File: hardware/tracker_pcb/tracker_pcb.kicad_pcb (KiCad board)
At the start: 4 copper layers, 132.8 x 54.5 mm, 99 parts, among them IC1 DRV8244SQRYJRQ1, IC2 DRV8244SQRYJRQ1, IC3 THVD1426DRLR, IC4 WIO-SX1262, J1 JL308-25412G01, J2 B6B-PH-K-S, J3 256-406, J4 USB_C_Receptacle_USB2.0_16P, J5 B4B-XH-A, Q1 LTV-817S-TA1-D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

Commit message: wip
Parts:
- removed U2: STPS30L30DJF-TR, footprint:SON_0L30DJF-TR_STM
- added CR1: V60D60C-M3/I, footprint:DPAK_60C-M3&slash_I_VIS, F.Cu at (97.6, 91.9)
- moved U4 8.27 mm to (90.3, 68.6), turned to 0 degrees
- moved C6 4.32 mm to (98.2, 77.0), turned to 0 degrees
- moved R3 3.18 mm to (90.1, 72.3)
- moved R2 3.16 mm to (90.1, 70.7)
- moved R6 1.98 mm to (95.9, 69.0), turned to -90 degrees
- moved D2 1.30 mm to (97.6, 69.0), turned to 90 degrees
- moved X1 0.25 mm to (92.5, 108.0)
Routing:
- net Net-(U4-VIN2): track 43.4 -> 56.2 mm, vias 0 -> 3
- net /VBUS: track 102.3 -> 114.4 mm, vias 5 -> 6
- net Net-(U4-PR1): track 9.34 -> 3.05 mm, vias 2 -> 0
- net VDD: track 56.3 -> 60.4 mm
- net GND: track 5.16 -> 7.30 mm, vias 288 -> 293
- net VRPP: vias 117 -> 114
- net /Power/VRAW: vias 0 -> 10
- added copper zone on B.Cu, net /Power/VRAW
- added copper zone on In2.Cu, net /Power/VRAW
- removed copper zone on F.Cu, net VDD

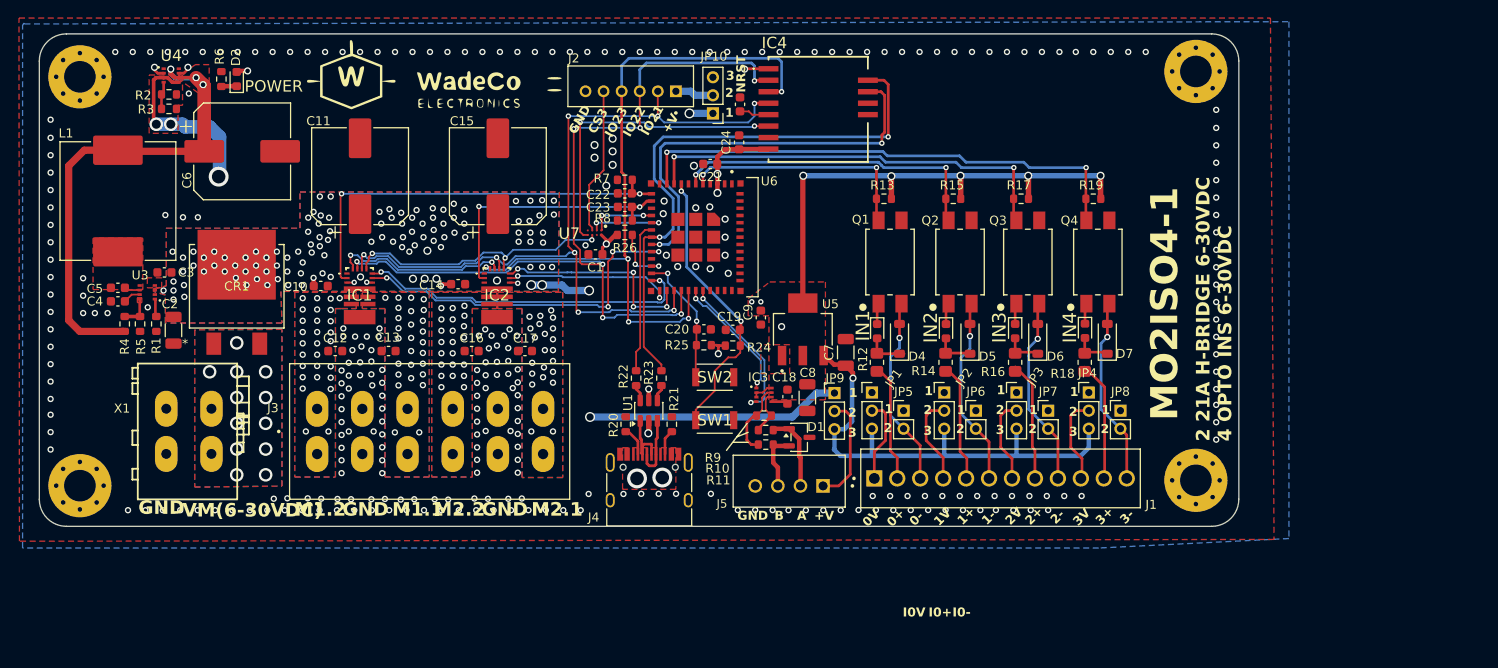
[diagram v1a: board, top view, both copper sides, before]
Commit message: Add jst xh for inputs
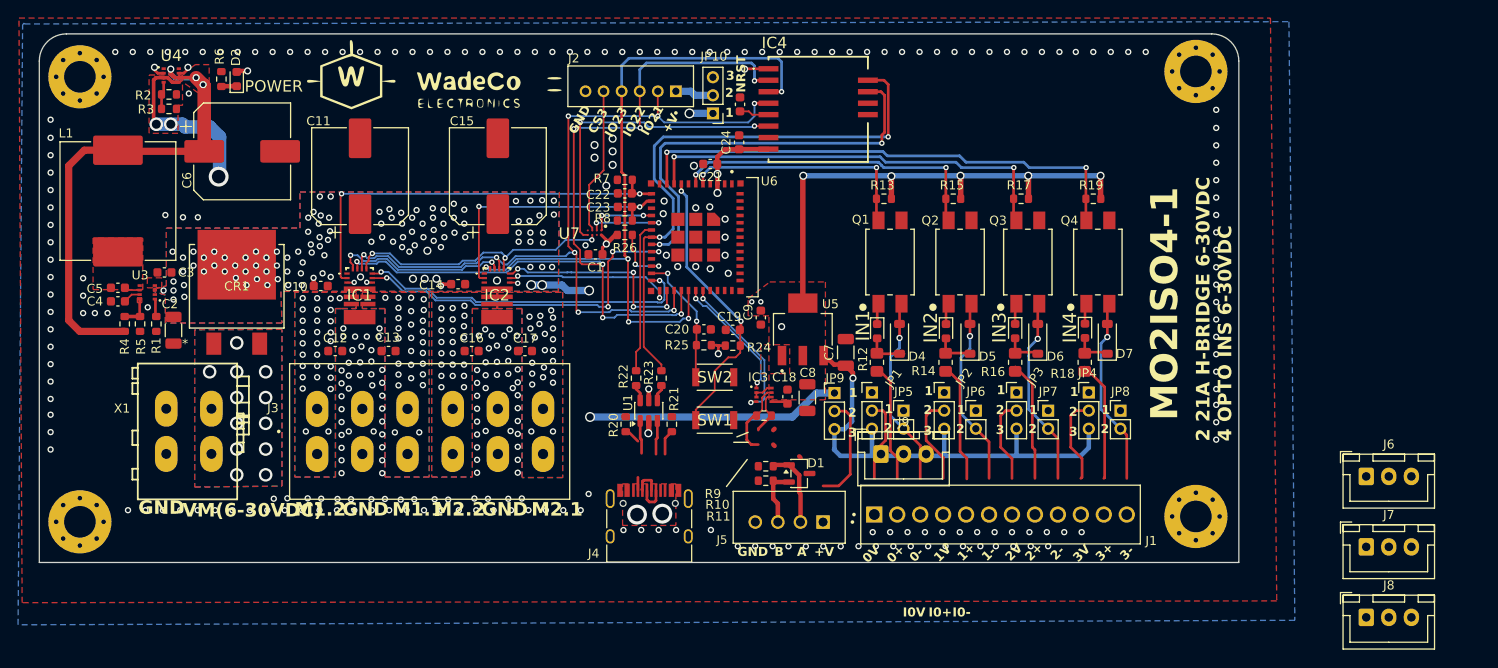
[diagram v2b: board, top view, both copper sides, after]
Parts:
- added J6: B3B-XH-A(LF)(SN), Connector_JST:JST_XH_B3B-XH-A_1x03_P2.50mm_Vertical, F.Cu at (222.6, 113.0)
- added J7: B3B-XH-A(LF)(SN), Connector_JST:JST_XH_B3B-XH-A_1x03_P2.50mm_Vertical, F.Cu at (222.6, 120.8)
- added J8: B3B-XH-A(LF)(SN), Connector_JST:JST_XH_B3B-XH-A_1x03_P2.50mm_Vertical, F.Cu at (222.6, 128.6)
- added J9: B3B-XH-A(LF)(SN), Connector_JST:JST_XH_B3B-XH-A_1x03_P2.50mm_Vertical, F.Cu at (168.9, 110.5)
- moved D1 4.00 mm to (159.8, 112.7)
- moved H2 4.00 mm to (203.8, 117.4)
- moved H3 4.00 mm to (80.2, 118.0)
- moved J1 4.00 mm to (182.1, 117.2)
- moved J4 4.00 mm to (143.2, 118.6)
- moved J5 4.00 mm to (158.7, 117.5)
- moved R10 4.00 mm to (156.2, 111.8)
- moved R11 4.00 mm to (156.2, 113.5)
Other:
- board size 132.8 x 54.5 mm -> 132.8 x 58.5 mm

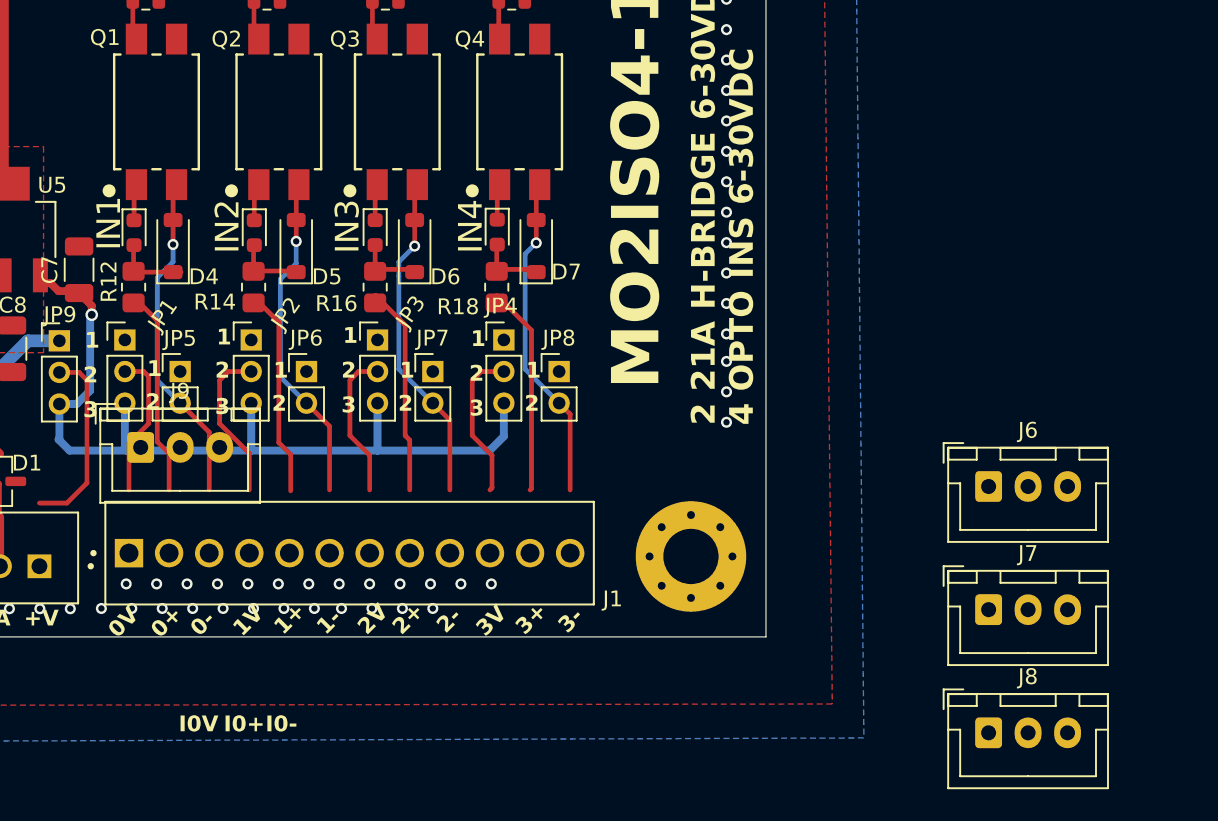
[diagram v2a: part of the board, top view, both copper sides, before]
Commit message: Add "hardware interlock" option to use iso ins 1-4 as hardware interlock for HBRDIGE PWM signals
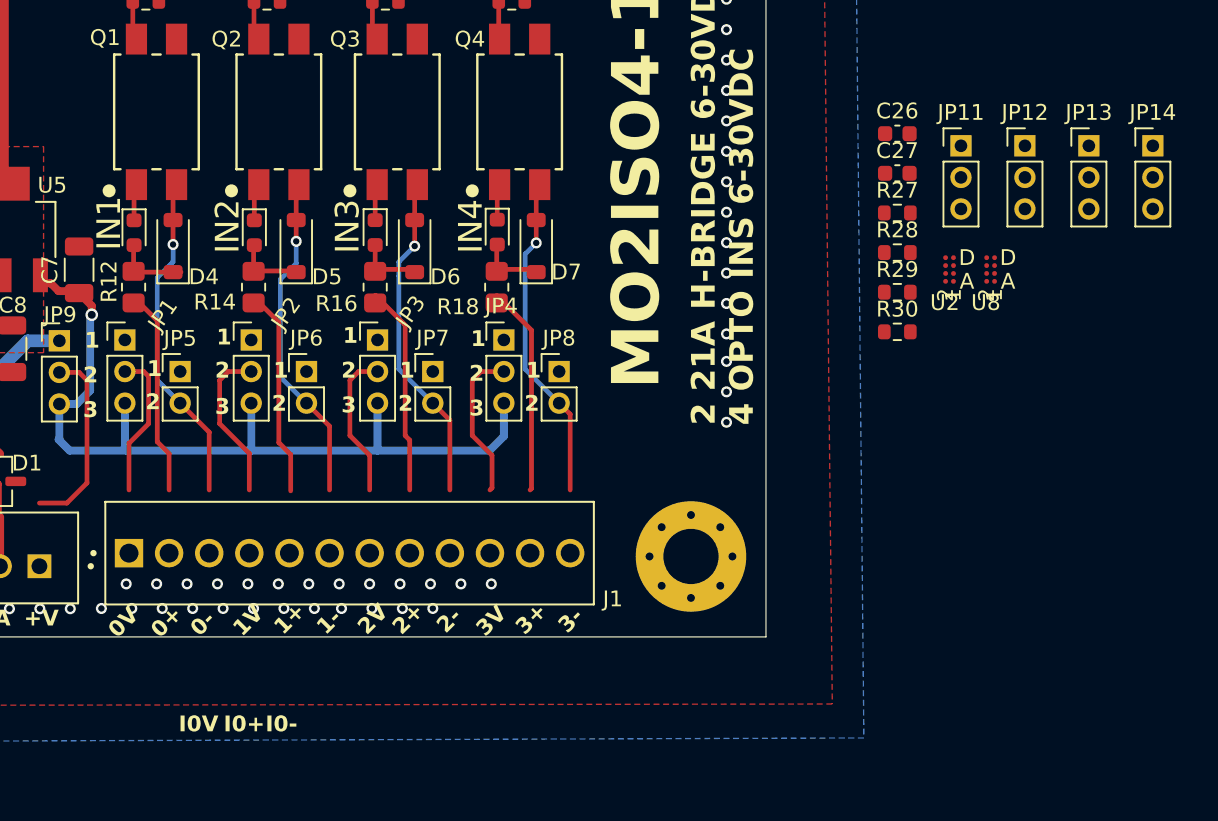
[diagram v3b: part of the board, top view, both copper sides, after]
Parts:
- removed J6, J7, J8, J9: B3B-XH-A(LF)(SN), Connector_JST:JST_XH_B3B-XH-A_1x03_P2.50mm_Vertical
- added C26: 100nF, Capacitor_SMD:C_0603_1608Metric, F.Cu at (216.8, 90.6)
- added C27: 100nF, Capacitor_SMD:C_0603_1608Metric, F.Cu at (216.8, 93.1)
- added JP11: Jumper_3_Open, Connector_PinHeader_2.00mm:PinHeader_1x03_P2.00mm_Vertical, F.Cu at (220.8, 91.4)
- added JP12: Jumper_3_Open, Connector_PinHeader_2.00mm:PinHeader_1x03_P2.00mm_Vertical, F.Cu at (224.9, 91.4)
- added JP13: Jumper_3_Open, Connector_PinHeader_2.00mm:PinHeader_1x03_P2.00mm_Vertical, F.Cu at (228.9, 91.4)
- added JP14: Jumper_3_Open, Connector_PinHeader_2.00mm:PinHeader_1x03_P2.00mm_Vertical, F.Cu at (233.0, 91.4)
- added R27: 47k, Resistor_SMD:R_0603_1608Metric, F.Cu at (216.8, 95.7)
- added R28: 47k, Resistor_SMD:R_0603_1608Metric, F.Cu at (216.8, 98.2)
- added R29: 47k, Resistor_SMD:R_0603_1608Metric, F.Cu at (216.8, 100.7)
- added R30: 47k, Resistor_SMD:R_0603_1608Metric, F.Cu at (216.8, 103.2)
- added U2: SN74AUP2G125YZPR, footprint:YZP8, F.Cu at (220.1, 99.2)
- added U8: SN74AUP2G125YZPR, footprint:YZP8, F.Cu at (222.7, 99.2)
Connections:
- net /Isolated Input/ISO_GPIO renamed /ISO0
- net /Isolated Input1/ISO_GPIO renamed /ISO1
- net /Isolated Input2/ISO_GPIO renamed /ISO2
- net /Isolated Input3/ISO_GPIO renamed /ISO3
- IC1 pad 11: /M1PWMF -> /Motor Control DRV8244_1/PWMF
- IC1 pad 12: /M1PWMR -> /Motor Control DRV8244_1/PWMR
- IC2 pad 11: /M2PWMF -> /Motor Control DRV8244_2/PWMF
- IC2 pad 12: /M2PWMR -> /Motor Control DRV8244_2/PWMR

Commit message: ss changes
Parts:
- removed C22, C23, C27: 100nF, Capacitor_SMD:C_0603_1608Metric
- removed R8: 820R, Resistor_SMD:R_0603_1608Metric
- added D3: LED, LED_SMD:LED_0603_1608Metric, F.Cu at (119.3, 86.7)
- R7: value 820R -> 460
- moved U8 84.0 mm to (139.1, 91.1), turned to 180 degrees
- moved U2 80.4 mm to (139.7, 99.5), turned to 180 degrees
- moved R28 78.2 mm to (138.7, 95.1), turned to 90 degrees
- moved R27 78.0 mm to (139.2, 103.6), turned to 90 degrees
- moved R30 76.9 mm to (140.3, 95.1), turned to 90 degrees
- moved C26 76.1 mm to (141.0, 97.4)
- moved R29 76.1 mm to (140.8, 103.6), turned to 90 degrees
- moved JP12 63.2 mm to (161.8, 89.8), turned to 180 degrees
- moved JP13 63.2 mm to (165.8, 89.8), turned to 180 degrees
- moved JP11 63.1 mm to (157.8, 89.8), turned to 180 degrees
- moved JP14 63.1 mm to (169.9, 89.8), turned to 180 degrees
- moved R7 21.3 mm to (119.3, 78.9), turned to 90 degrees
- moved R13 6.18 mm to (175.4, 82.2)
- moved D4 5.01 mm to (176.0, 97.6)
- moved LED1 5.01 mm to (173.5, 96.8)
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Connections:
- net /RS485/rs485_rx renamed /ESP32-C6/RXD0
- net /RS485/rs485_tx renamed /ESP32-C6/TXD0
- net /esp32/IO6 renamed /ESP32-C6/IO6
- net /esp32/IO7 renamed /ESP32-C6/IO7
- net /esp32/NSS_CS0 renamed /ESP32-C6/NSS_CS0
- net /esp32/USB_DM renamed /ESP32-C6/USB_DM
- C26 pad 1: GND -> V33
- C26 pad 2: V33 -> GND
- IC1 pad 1: unconnected-(IC1-NFAULT-Pad1) -> /NFAULT
- IC1 pad 2: /IOUT1 -> GND
- IC2 pad 1: unconnected-(IC2-NFAULT-Pad1) -> /NFAULT
- IC2 pad 2: /IOUT2 -> GND
- JP12 pad 2: /~{HIL0} -> /~{HIL1}
- JP12 pad 3: /ISO0 -> /ISO1
- JP13 pad 2: /~{HIL0} -> /~{HIL2}
- JP13 pad 3: /ISO0 -> /ISO2
- JP14 pad 2: /~{HIL0} -> /~{HIL3}
- JP14 pad 3: /ISO0 -> /ISO3
- R7 pad 1: GND -> Net-(D3-A)
- R7 pad 2: /IOUT1 -> VDD
- U6 pad 12: /IOUT1 -> /SX_RST
- U6 pad 13: /IOUT2 -> /NFAULT
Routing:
- net VDD: track 60.4 -> 12.1 mm, vias 5 -> 6
- net /IOUT1: track 46.7 -> 0.00 mm, vias 2 -> 0
- net /NFAULT: track 0.00 -> 44.6 mm, vias 0 -> 4
- net /Motor Control DRV8244_1/PWMF: track 0.00 -> 43.2 mm, vias 0 -> 2
- net /Motor Control DRV8244_1/PWMR: track 0.00 -> 37.7 mm, vias 0 -> 2
- net /~{HIL1}: track 0.00 -> 35.7 mm, vias 0 -> 2
- net /~{HIL3}: track 0.00 -> 32.0 mm, vias 0 -> 1
- net /IOUT2: track 30.6 -> 0.00 mm, vias 2 -> 0
- net /~{HIL0}: track 0.00 -> 30.0 mm, vias 0 -> 2
- net /~{HIL2}: track 0.00 -> 29.7 mm, vias 0 -> 1
- net /M1PWMR: track 37.3 -> 17.3 mm, vias 2 -> 4
- net /SX_RST: track 3.30 -> 22.8 mm, vias 0 -> 2
- net V33: track 119.7 -> 139.2 mm, vias 13 -> 14
- net /M1PWMF: track 39.6 -> 22.0 mm, vias 4 -> 3
- net /Motor Control DRV8244_2/PWMF: track 0.00 -> 17.3 mm, vias 0 -> 2
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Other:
- board size 132.8 x 58.5 mm -> 131.2 x 58.1 mm
- board text added: "--M1--"
- board text added: "--M2--"
- board text added: "4"
- board text added: "BOOT"
- board text added: "FAULT"
- board text added: "HARDWARE INTERLOCK"
- board text added: "RESET"
- board text added: "V1"
- board text added: "V2"
- board text added: "V3"
- board text added: "V4"
- board text added: "{+}"
- board text added: "{-}"
- board text removed: "0+"
- board text removed: "0-"
- board text removed: "0V"
- board text removed: "1+"
- board text removed: "1-"
- board text removed: "1V"
- board text removed: "2+"
- board text removed: "2-"
- board text removed: "2V"
- board text removed: "3+"
- board text removed: "3-"
- board text removed: "3V"
- board text removed: "I0+"
- board text removed: "I0-"
- board text removed: "I0V"
- board text removed: "MO2ISO4-1"
